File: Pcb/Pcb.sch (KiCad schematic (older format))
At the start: 120 parts, among them J1 ISP, J2 TRRS, Q1 2N7002, SW1 SW_Push, SW10 SW_Push, SW11 SW_Push, SW12 SW_Push, SW13 SW_Push, SW14 SW_Push, SW15 SW_Push, SW16 SW_Push, SW17 SW_Push, SW18 SW_Push, SW19 SW_Push, SW2 SW2, SW20 SW_Push, SW21 SW_Push, SW22 SW_Push, SW23 SW_Push, SW24 SW_Push, SW25 SW_Push, SW26 SW_Push, SW27 SW_Push, SW28 SW_Push, SW29 SW_Push, SW3 SW_Push, SW4 SW_Push, SW5 SW_Push, SW6 SW_Push, SW7 SW_Push, SW8 SW_Push, SW9 SW_Push, U1 ProMicro

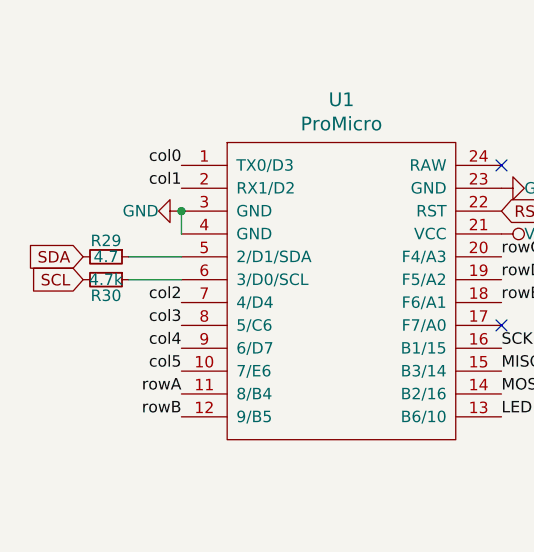
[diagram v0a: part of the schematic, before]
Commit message: Fixed bug with I2C resistor's
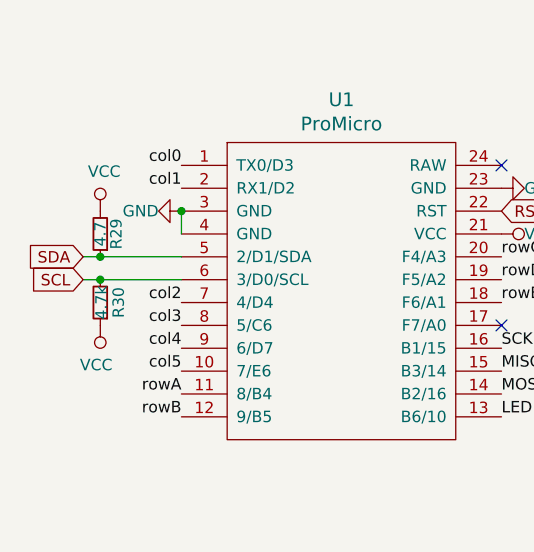
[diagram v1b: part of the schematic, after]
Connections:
- net SCL: now also U1.6 (3/D0/SCL)
- net SDA: now also R29.1, U1.5 (2/D1/SDA); no longer R29.2
- net VCC: now also R29.2, R30.1
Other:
- moved on the sheet: R29, R30
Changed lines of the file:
@@
 L Device:R_Small R29
 U 1 1 5DAAA6F2
-P 1075 1725
-F 0 "R29" V 1005 1725 50  0000 C CNN
-F 1 "4.7" V 1075 1725 50  0000 C CNN
-F 2 "Used_Footprints:Resistor_SMD_TH" H 1075 1725 50  0001 C CNN
-F 3 "~" H 1075 1725 50  0001 C CNN
-	1    1075 1725
-	0    1    1    0
+P 1050 1625
+F 0 "R29" V 980 1625 50  0000 C CNN
+F 1 "4.7" V 1050 1625 50  0000 C CNN
+F 2 "Used_Footprints:Resistor_SMD_TH" H 1050 1625 50  0001 C CNN
+F 3 "~" H 1050 1625 50  0001 C CNN
+	1    1050 1625
+	-1   0    0    1
 $EndComp
 $Comp
 L Device:R_Small R30
 U 1 1 5DAAB292
-P 1075 1825
-F 0 "R30" V 1145 1825 50  0000 C CNN
-F 1 "4.7k" V 1075 1825 50  0000 C CNN
-F 2 "Used_Footprints:Resistor_SMD_TH" H 1075 1825 50  0001 C CNN
-F 3 "~" H 1075 1825 50  0001 C CNN
-	1    1075 1825
-	0    1    1    0
-$EndComp
-Wire Wire Line
-	1175 1725 1405 1725
-Wire Wire Line
-	1175 1825 1405 1825
+P 1050 1925
+F 0 "R30" V 970 1925 50  0000 C CNN
+F 1 "4.7k" V 1045 1925 50  0000 C CNN
+F 2 "Used_Footprints:Resistor_SMD_TH" H 1050 1925 50  0001 C CNN
+F 3 "~" H 1050 1925 50  0001 C CNN
+	1    1050 1925
+	-1   0    0    1
+$EndComp
 Text GLabel 975  1725 0    50   Input ~ 0
 SDA
@@
 	0    -1   -1   0
 $EndComp
+Wire Wire Line
+	975  1725 1050 1725
+Wire Wire Line
+	975  1825 1050 1825
+Connection ~ 1050 1825
+Wire Wire Line
+	1050 1825 1405 1825
+Connection ~ 1050 1725
+Wire Wire Line
+	1050 1725 1405 1725
+$Comp
+L power:VCC #PWR?
+U 1 1 5DBF6680
+P 1050 1525
+F 0 "#PWR?" H 1050 1375 50  0001 C CNN
+F 1 "VCC" H 1067 1698 50  0000 C CNN
+F 2 "" H 1050 1525 50  0001 C CNN
+F 3 "" H 1050 1525 50  0001 C CNN
+	1    1050 1525
+	1    0    0    -1
+$EndComp
+$Comp
+L power:VCC #PWR?
+U 1 1 5DBF75FF
+P 1050 2025
+F 0 "#PWR?" H 1050 1875 50  0001 C CNN
+F 1 "VCC" H 1068 2198 50  0000 C CNN
+F 2 "" H 1050 2025 50  0001 C CNN
+F 3 "" H 1050 2025 50  0001 C CNN
+	1    1050 2025
+	-1   0    0    1
+$EndComp
 $EndSCHEMATC

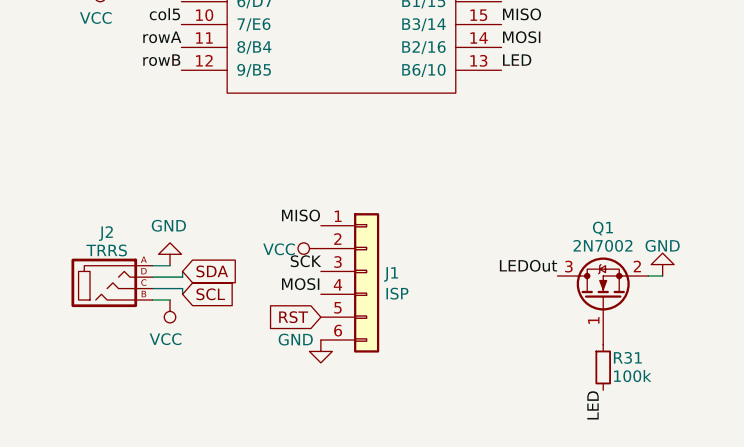
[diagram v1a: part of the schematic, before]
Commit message: Deleted ISP header
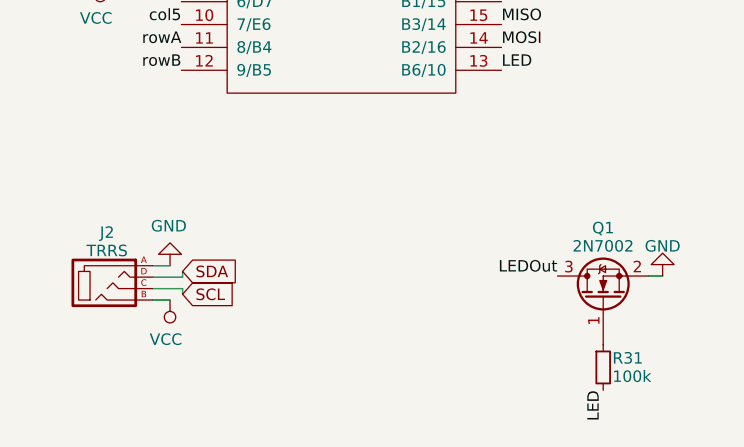
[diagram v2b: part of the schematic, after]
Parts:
- removed J1: ISP, Used_Footprints:ISP, symbol Connector_Generic:Conn_01x06
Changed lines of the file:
@@
 Wire Wire Line
 	1410 3330 1410 3305
-$Comp
-L Connector_Generic:Conn_01x06 J1
-U 1 1 5DC27926
-P 2215 3305
-F 0 "J1" H 2295 3297 50  0000 L CNN
-F 1 "ISP" H 2295 3206 50  0000 L CNN
-F 2 "Used_Footprints:ISP" H 2215 3305 50  0001 C CNN
-F 3 "~" H 2215 3305 50  0001 C CNN
-	1    2215 3305
-	1    0    0    -1
-$EndComp
-Text Label 2015 3105 2    50   ~ 0
-MISO
-Text Label 2015 3305 2    50   ~ 0
-SCK
-Text Label 2015 3405 2    50   ~ 0
-MOSI
-Text GLabel 2015 3505 0    50   Input ~ 0
-RST
 Text GLabel 4605 3615 0    50   Input ~ 0
 RST
 Text GLabel 2805 1525 2    50   Input ~ 0
 RST
-$Comp
-L power:GND #PWR011
-U 1 1 5DC2E762
-P 2015 3605
-F 0 "#PWR011" H 2015 3355 50  0001 C CNN
-F 1 "GND" H 1905 3605 50  0000 C CNN
-F 2 "" H 2015 3605 50  0001 C CNN
-F 3 "" H 2015 3605 50  0001 C CNN
-	1    2015 3605
-	1    0    0    -1
-$EndComp
-$Comp
-L power:VCC #PWR08
-U 1 1 5DC2FF16
-P 2015 3205
-F 0 "#PWR08" H 2015 3055 50  0001 C CNN
-F 1 "VCC" V 2010 3315 50  0000 L CNN
-F 2 "" H 2015 3205 50  0001 C CNN
-F 3 "" H 2015 3205 50  0001 C CNN
-	1    2015 3205
-	0    -1   -1   0
-$EndComp
 Wire Wire Line
 	975  1725 1050 1725

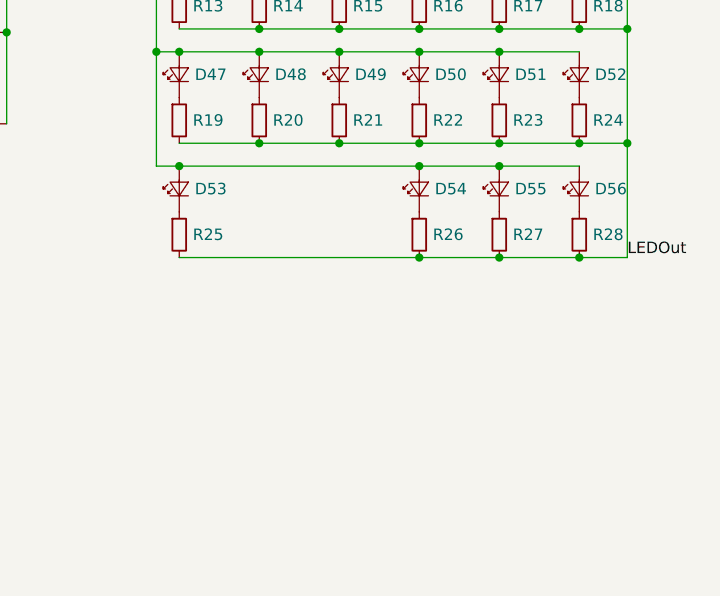
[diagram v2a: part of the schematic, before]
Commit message: Added LED's for lock indication
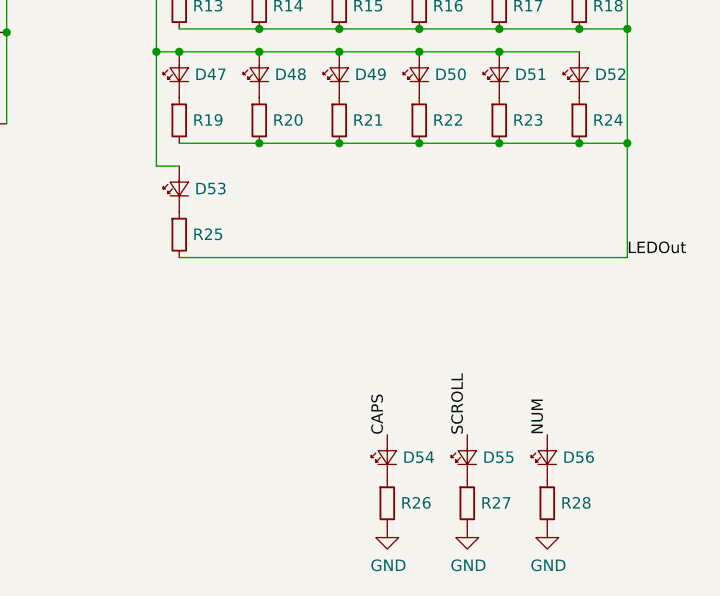
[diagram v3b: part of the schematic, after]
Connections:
- net GND: now also R26.2, R27.2, R28.2
- net LEDOut: no longer R26.2, R27.2, R28.2
- net VCC: no longer D54.2 (A), D55.2 (A), D56.2 (A)
- new net CAPS: D54.2 (A)
- new net NUM: D56.2 (A)
- new net SCROLL: D55.2 (A)
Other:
- moved on the sheet: D54, D55, D56, R26, R27, R28
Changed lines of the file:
@@
 L Device:LED_Small D54
 U 1 1 5DB0079C
-P 9590 3005
-F 0 "D54" V 9590 2937 50  0000 R CNN
-F 1 "LED_Small" V 9545 2937 50  0001 R CNN
-F 2 "Used_Footprints:LED" V 9590 3005 50  0001 C CNN
-F 3 "~" V 9590 3005 50  0001 C CNN
-	1    9590 3005
+P 9450 4180
+F 0 "D54" V 9450 4112 50  0000 R CNN
+F 1 "LED_Small" V 9405 4112 50  0001 R CNN
+F 2 "Used_Footprints:LED" V 9450 4180 50  0001 C CNN
+F 3 "~" V 9450 4180 50  0001 C CNN
+	1    9450 4180
 	0    -1   -1   0
 $EndComp
@@
 L Device:LED_Small D55
 U 1 1 5DB007A2
-P 9940 3005
-F 0 "D55" V 9940 2937 50  0000 R CNN
-F 1 "LED_Small" V 9895 2937 50  0001 R CNN
-F 2 "Used_Footprints:LED" V 9940 3005 50  0001 C CNN
-F 3 "~" V 9940 3005 50  0001 C CNN
-	1    9940 3005
+P 9800 4180
+F 0 "D55" V 9800 4112 50  0000 R CNN
+F 1 "LED_Small" V 9755 4112 50  0001 R CNN
+F 2 "Used_Footprints:LED" V 9800 4180 50  0001 C CNN
+F 3 "~" V 9800 4180 50  0001 C CNN
+	1    9800 4180
 	0    -1   -1   0
 $EndComp
@@
 L Device:LED_Small D56
 U 1 1 5DB007A8
-P 10290 3005
-F 0 "D56" V 10290 2937 50  0000 R CNN
-F 1 "LED_Small" V 10245 2937 50  0001 R CNN
-F 2 "Used_Footprints:LED" V 10290 3005 50  0001 C CNN
-F 3 "~" V 10290 3005 50  0001 C CNN
-	1    10290 3005
+P 10150 4180
+F 0 "D56" V 10150 4112 50  0000 R CNN
+F 1 "LED_Small" V 10105 4112 50  0001 R CNN
+F 2 "Used_Footprints:LED" V 10150 4180 50  0001 C CNN
+F 3 "~" V 10150 4180 50  0001 C CNN
+	1    10150 4180
 	0    -1   -1   0
 $EndComp
@@
 L Device:R_Small R26
 U 1 1 5DB007C0
-P 9590 3205
-F 0 "R26" H 9649 3205 50  0000 L CNN
-F 1 "R_Small" H 9649 3160 50  0001 L CNN
-F 2 "Used_Footprints:Resistor_SMD_TH" H 9590 3205 50  0001 C CNN
-F 3 "~" H 9590 3205 50  0001 C CNN
-	1    9590 3205
+P 9450 4380
+F 0 "R26" H 9509 4380 50  0000 L CNN
+F 1 "R_Small" H 9509 4335 50  0001 L CNN
+F 2 "Used_Footprints:Resistor_SMD_TH" H 9450 4380 50  0001 C CNN
+F 3 "~" H 9450 4380 50  0001 C CNN
+	1    9450 4380
 	1    0    0    -1
 $EndComp
@@
 L Device:R_Small R27
 U 1 1 5DB007C6
-P 9940 3205
-F 0 "R27" H 9999 3205 50  0000 L CNN
-F 1 "R_Small" H 9999 3160 50  0001 L CNN
-F 2 "Used_Footprints:Resistor_SMD_TH" H 9940 3205 50  0001 C CNN
-F 3 "~" H 9940 3205 50  0001 C CNN
-	1    9940 3205
+P 9800 4380
+F 0 "R27" H 9859 4380 50  0000 L CNN
+F 1 "R_Small" H 9859 4335 50  0001 L CNN
+F 2 "Used_Footprints:Resistor_SMD_TH" H 9800 4380 50  0001 C CNN
+F 3 "~" H 9800 4380 50  0001 C CNN
+	1    9800 4380
 	1    0    0    -1
 $EndComp
@@
 L Device:R_Small R28
 U 1 1 5DB007CC
-P 10290 3205
-F 0 "R28" H 10349 3205 50  0000 L CNN
-F 1 "R_Small" H 10349 3160 50  0001 L CNN
-F 2 "Used_Footprints:Resistor_SMD_TH" H 10290 3205 50  0001 C CNN
-F 3 "~" H 10290 3205 50  0001 C CNN
-	1    10290 3205
+P 10150 4380
+F 0 "R28" H 10209 4380 50  0000 L CNN
+F 1 "R_Small" H 10209 4335 50  0001 L CNN
+F 2 "Used_Footprints:Resistor_SMD_TH" H 10150 4380 50  0001 C CNN
+F 3 "~" H 10150 4380 50  0001 C CNN
+	1    10150 4380
 	1    0    0    -1
 $EndComp
@@
 Wire Wire Line
 	9940 2805 9590 2805
-Wire Wire Line
-	8540 2905 9590 2905
-Connection ~ 9590 2905
-Wire Wire Line
-	9590 2905 9940 2905
-Connection ~ 9940 2905
-Wire Wire Line
-	9940 2905 10290 2905
-Wire Wire Line
-	10290 3305 9940 3305
-Connection ~ 9590 3305
-Wire Wire Line
-	9590 3305 8540 3305
-Connection ~ 9940 3305
-Wire Wire Line
-	9940 3305 9590 3305
 Text Label 4785 1070 1    50   ~ 0
 col0
@@
 $EndComp
 Wire Wire Line
-	10500 3305 10290 3305
-Connection ~ 10290 3305
-Wire Wire Line
 	10290 2805 10500 2805
 Connection ~ 10290 2805
@@
 Wire Wire Line
 	8440 2905 8440 2405
-Connection ~ 8540 2905
 Wire Wire Line
 	8540 905  8440 905
@@
 	-1   0    0    1
 $EndComp
+Wire Wire Line
+	8540 3305 10500 3305
+$Comp
+L power:GND #PWR?
+U 1 1 5DC0A2E9
+P 9450 4480
+F 0 "#PWR?" H 9450 4230 50  0001 C CNN
+F 1 "GND" H 9455 4307 50  0000 C CNN
+F 2 "" H 9450 4480 50  0001 C CNN
+F 3 "" H 9450 4480 50  0001 C CNN
+	1    9450 4480
+	1    0    0    -1
+$EndComp
+$Comp
+L power:GND #PWR?
+U 1 1 5DC0B2EF
+P 9800 4480
+F 0 "#PWR?" H 9800 4230 50  0001 C CNN
+F 1 "GND" H 9805 4307 50  0000 C CNN
+F 2 "" H 9800 4480 50  0001 C CNN
+F 3 "" H 9800 4480 50  0001 C CNN
+	1    9800 4480
+	1    0    0    -1
+$EndComp
+$Comp
+L power:GND #PWR?
+U 1 1 5DC0C10E
+P 10150 4480
+F 0 "#PWR?" H 10150 4230 50  0001 C CNN
+F 1 "GND" H 10155 4307 50  0000 C CNN
+F 2 "" H 10150 4480 50  0001 C CNN
+F 3 "" H 10150 4480 50  0001 C CNN
+	1    10150 4480
+	1    0    0    -1
+$EndComp
+Text Label 9450 4080 1    50   ~ 0
+CAPS
+Text Label 9800 4080 1    50   ~ 0
+SCROLL
+Text Label 10150 4080 1    50   ~ 0
+NUM
 $EndSCHEMATC

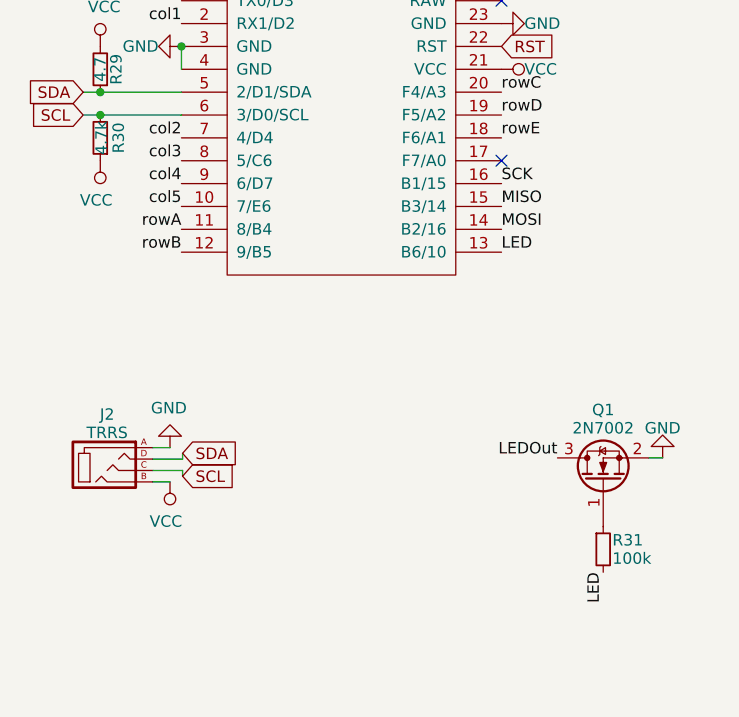
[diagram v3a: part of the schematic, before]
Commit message: Changed I2C jack
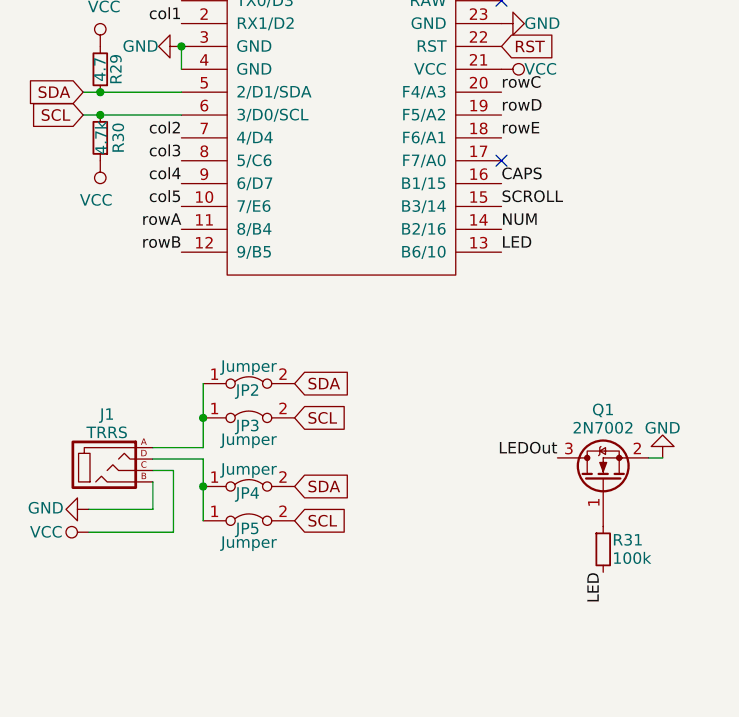
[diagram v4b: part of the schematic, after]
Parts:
- added JP2, JP3, JP4, JP5: Jumper, symbol Jumper:Jumper_2_Bridged
- renumbered J2 to J1
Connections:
- net MISO is gone; now on net SCROLL: U1.15 (B3/14)
- net MOSI is gone; now on net NUM: U1.14 (B2/16)
- net SCK is gone; now on net CAPS: U1.16 (B1/15)
- net GND: now also J1.B; no longer J1.A
- net SCL: now also JP3.2 (B), JP5.2 (B); no longer J1.C
- net SDA: now also JP2.2 (B), JP4.2 (B); no longer J1.D
- net VCC: now also J1.C; no longer J1.B
- new net: J1.A, JP2.1 (A), JP3.1 (A)
- new net: J1.D, JP4.1 (A), JP5.1 (A)
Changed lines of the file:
@@
 Text Label 2805 1925 0    50   ~ 0
 rowE
-Text Label 2805 2125 0    50   ~ 0
-SCK
-Text Label 2805 2225 0    50   ~ 0
-MISO
-Text Label 2805 2325 0    50   ~ 0
-MOSI
 Text Label 2805 2425 0    50   ~ 0
 LED
@@
 $EndComp
 $Comp
-L kbd:MJ-4PP-9 J2
+L kbd:MJ-4PP-9 J1
 U 1 1 5DBFACF7
 P 1080 3355
-F 0 "J2" H 1080 3575 50  0000 C CNN
+F 0 "J1" H 1080 3575 50  0000 C CNN
 F 1 "TRRS" H 1080 3495 50  0000 C CNN
 F 2 "Used_Footprints:TRRS_2Side" H 1355 3530 50  0001 C CNN
@@
 	1    0    0    -1
 $EndComp
-$Comp
-L power:GND #PWR09
-U 1 1 5DBFC00F
-P 1355 3280
-F 0 "#PWR09" H 1355 3030 50  0001 C CNN
-F 1 "GND" H 1360 3107 50  0000 C CNN
-F 2 "" H 1355 3280 50  0001 C CNN
-F 3 "" H 1355 3280 50  0001 C CNN
-	1    1355 3280
-	-1   0    0    1
-$EndComp
-$Comp
-L power:VCC #PWR010
-U 1 1 5DBFD01C
-P 1355 3430
-F 0 "#PWR010" H 1355 3280 50  0001 C CNN
-F 1 "VCC" H 1373 3603 50  0000 C CNN
-F 2 "" H 1355 3430 50  0001 C CNN
-F 3 "" H 1355 3430 50  0001 C CNN
-	1    1355 3430
-	-1   0    0    1
-$EndComp
-Wire Wire Line
-	1280 3430 1355 3430
-Wire Wire Line
-	1280 3280 1355 3280
-Text GLabel 1410 3305 2    50   Input ~ 0
-SDA
-Text GLabel 1410 3405 2    50   Input ~ 0
-SCL
-Wire Wire Line
-	1280 3380 1410 3380
-Wire Wire Line
-	1410 3380 1410 3405
-Wire Wire Line
-	1280 3330 1410 3330
-Wire Wire Line
-	1410 3330 1410 3305
 Text GLabel 4605 3615 0    50   Input ~ 0
 RST
@@
 Text Label 10150 4080 1    50   ~ 0
 NUM
+Text Label 2805 2125 0    50   ~ 0
+CAPS
+Text Label 2805 2225 0    50   ~ 0
+SCROLL
+Text Label 2805 2325 0    50   ~ 0
+NUM
+$Comp
+L power:GND #PWR?
+U 1 1 5DC1A713
+P 1000 3550
+F 0 "#PWR?" H 1000 3300 50  0001 C CNN
+F 1 "GND" V 995 3440 50  0000 R CNN
+F 2 "" H 1000 3550 50  0001 C CNN
+F 3 "" H 1000 3550 50  0001 C CNN
+	1    1000 3550
+	0    1    1    0
+$EndComp
+$Comp
+L power:VCC #PWR?
+U 1 1 5DC1BBEB
+P 1000 3650
+F 0 "#PWR?" H 1000 3500 50  0001 C CNN
+F 1 "VCC" V 1000 3765 50  0000 L CNN
+F 2 "" H 1000 3650 50  0001 C CNN
+F 3 "" H 1000 3650 50  0001 C CNN
+	1    1000 3650
+	0    -1   -1   0
+$EndComp
+Wire Wire Line
+	1280 3430 1280 3550
+Wire Wire Line
+	1280 3550 1000 3550
+Wire Wire Line
+	1280 3380 1370 3380
+Wire Wire Line
+	1370 3380 1370 3650
+Wire Wire Line
+	1370 3650 1000 3650
+$Comp
+L Jumper:Jumper_2_Bridged JP4
+U 1 1 5DC2DEC8
+P 1700 3450
+F 0 "JP4" H 1695 3420 50  0000 C CNN
+F 1 "Jumper" H 1700 3525 50  0000 C CNN
+F 2 "" H 1700 3450 50  0001 C CNN
+F 3 "~" H 1700 3450 50  0001 C CNN
+	1    1700 3450
+	1    0    0    -1
+$EndComp
+$Comp
+L Jumper:Jumper_2_Bridged JP5
+U 1 1 5DC322E4
+P 1700 3600
+F 0 "JP5" H 1695 3565 50  0000 C CNN
+F 1 "Jumper" H 1700 3505 50  0000 C CNN
+F 2 "" H 1700 3600 50  0001 C CNN
+F 3 "~" H 1700 3600 50  0001 C CNN
+	1    1700 3600
+	1    0    0    -1
+$EndComp
+$Comp
+L Jumper:Jumper_2_Bridged JP2
+U 1 1 5DC382C2
+P 1700 3000
+F 0 "JP2" H 1695 2970 50  0000 C CNN
+F 1 "Jumper" H 1700 3075 50  0000 C CNN
+F 2 "" H 1700 3000 50  0001 C CNN
+F 3 "~" H 1700 3000 50  0001 C CNN
+	1    1700 3000
+	1    0    0    -1
+$EndComp
+$Comp
+L Jumper:Jumper_2_Bridged JP3
+U 1 1 5DC382C8
+P 1700 3150
+F 0 "JP3" H 1695 3115 50  0000 C CNN
+F 1 "Jumper" H 1700 3055 50  0000 C CNN
+F 2 "" H 1700 3150 50  0001 C CNN
+F 3 "~" H 1700 3150 50  0001 C CNN
+	1    1700 3150
+	1    0    0    -1
+$EndComp
+Wire Wire Line
+	1280 3330 1500 3330
+Wire Wire Line
+	1500 3330 1500 3450
+Connection ~ 1500 3450
+Wire Wire Line
+	1500 3450 1500 3600
+Wire Wire Line
+	1280 3280 1500 3280
+Wire Wire Line
+	1500 3280 1500 3150
+Connection ~ 1500 3150
+Wire Wire Line
+	1500 3150 1500 3000
+Text GLabel 1900 3000 2    50   Input ~ 0
+SDA
+Text GLabel 1900 3150 2    50   Input ~ 0
+SCL
+Text GLabel 1900 3450 2    50   Input ~ 0
+SDA
+Text GLabel 1900 3600 2    50   Input ~ 0
+SCL
 $EndSCHEMATC

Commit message: Updated footprints
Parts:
- J1: footprint Used_Footprints:TRRS_2Side -> 1symblos:MJ-4PP-9_Dual
- JP2, JP3, JP4, JP5: footprint (none) -> 1kbd:jumper
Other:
- moved on the sheet: D1, D10, D11, D12, D13, D14, D15, D16, D17, D18, D19, D2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
